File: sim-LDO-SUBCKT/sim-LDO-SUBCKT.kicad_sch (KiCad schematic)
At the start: 10 parts, among them U1 TLV76701DRVx

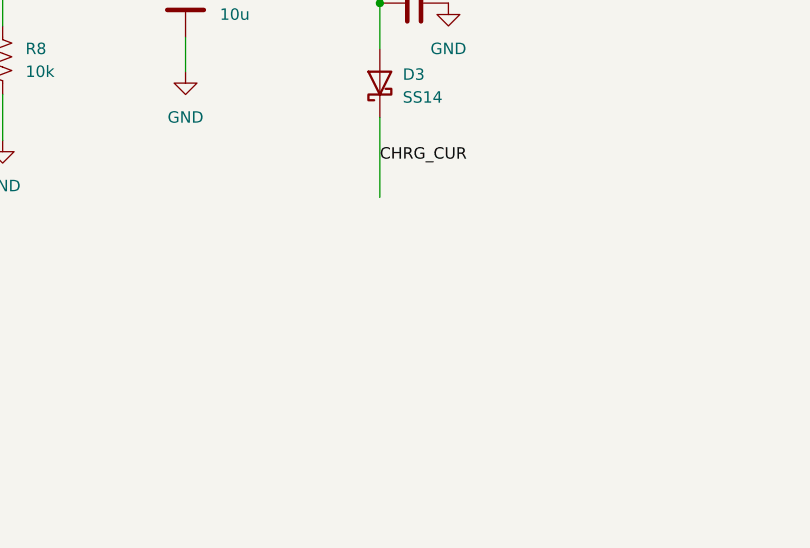
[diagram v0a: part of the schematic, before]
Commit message: simulations fixed with solid model files, results documented
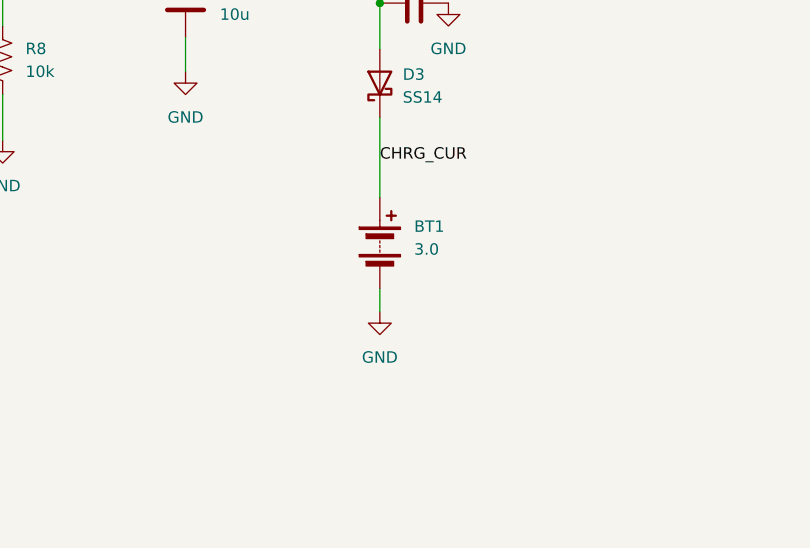
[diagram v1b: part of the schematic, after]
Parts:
- added BT1: 3.0, symbol Device:Battery
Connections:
- net CHRG_CUR: now also BT1.1 (+)
- net GND: now also BT1.2 (-)
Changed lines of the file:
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@@
+	(wire
+		(pts
+			(xy 175.26 127) (xy 175.26 129.54)
+		)
+		(stroke
+			(width 0)
+			(type default)
+		)
+	)
 	(wire
 		(pts
@@
 			)
 		)
-		(property "Sim.Library" "models/TLV767.txt"
+		(property "Sim.Library" "models/TLV76701P_ngspice.lib"
+			(at 116.84 91.44 0)
+			(hide yes)
+			(show_name no)
+			(do_not_autoplace no)
+			(effects
+				(font
+					(size 1.27 1.27)
+				)
+			)
+		)
+		(property "Sim.Name" "TLV76701_TRANS"
+			(at 116.84 91.44 0)
+			(hide yes)
+			(show_name no)
+			(do_not_autoplace no)
+			(effects
+				(font
+					(size 1.27 1.27)
+				)
+			)
+		)
+		(property "Sim.Device" "SUBCKT"
+			(at 116.84 91.44 0)
+			(hide yes)
+			(show_name no)
+			(do_not_autoplace no)
+			(effects
+				(font
+					(size 1.27 1.27)
+				)
+			)
+		)
+		(property "Sim.Pins" "1=VOUT 2=FB 3=GND 4=EN 6=VIN"
 			(at 116.84 91.44 0)
 			(hide yes)
@@
 	)
 	(symbol
+		(lib_id "power:GND")
+		(at 175.26 129.54 0)
+		(unit 1)
+		(body_style 1)
+		(exclude_from_sim no)
+		(in_bom yes)
+		(on_board yes)
+		(in_pos_files yes)
+		(dnp no)
+		(fields_autoplaced yes)
+		(property "Reference" "#PWR06"
+			(at 175.26 135.89 0)
+			(hide yes)
+			(show_name no)
+			(do_not_autoplace no)
+			(effects
+				(font
+					(size 1.27 1.27)
+				)
+			)
+		)
+		(property "Value" "GND"
+			(at 175.26 134.62 0)
+			(show_name no)
+			(do_not_autoplace no)
+			(effects
+				(font
+					(size 1.27 1.27)
+				)
+			)
+		)
+		(property "Footprint" ""
+			(at 175.26 129.54 0)
+			(hide yes)
+			(show_name no)
+			(do_not_autoplace no)
+			(effects
+				(font
+					(size 1.27 1.27)
+				)
+			)
+		)
+		(property "Datasheet" ""
+			(at 175.26 129.54 0)
+			(hide yes)
+			(show_name no)
+			(do_not_autoplace no)
+			(effects
+				(font
+					(size 1.27 1.27)
+				)
+			)
+		)
+		(property "Description" "Power symbol creates a global label with name \"GND\" , ground"
+			(at 175.26 129.54 0)
+			(hide yes)
+			(show_name no)
+			(do_not_autoplace no)
+			(effects
+				(font
+					(size 1.27 1.27)
+				)
+			)
+		)
+		(pin "1"
+		)
+		(instances
+			(project "sim-LDO-SUBCKT"
+				(path "/d4bc50a2-e541-43a2-bfb4-d9a873a3012e"
+					(reference "#PWR06")
+					(unit 1)
+				)
+			)
+		)
+	)
+	(symbol
 		(lib_id "Device:R_US")
 		(at 162.56 85.09 270)
@@
 					(unit 1)
 				)
+			)
+		)
+	)
+	(symbol
+		(lib_id "Device:Battery")
+		(at 175.26 121.92 0)
+		(unit 1)
+		(body_style 1)
+		(exclude_from_sim no)
+		(in_bom yes)
+		(on_board yes)
+		(in_pos_files yes)
+		(dnp no)
+		(fields_autoplaced yes)
+		(property "Reference" "BT1"
+			(at 179.07 120.0784 0)
+			(show_name no)
+			(do_not_autoplace no)
+			(effects
+				(font
+					(size 1.27 1.27)
+				)
+				(justify left)
+			)
+		)
+		(property "Value" "3.0"
+			(at 179.07 122.6184 0)
+			(show_name no)
+			(do_not_autoplace no)
+			(effects
+				(font
+					(size 1.27 1.27)
+				)
+				(justify left)
+			)
+		)
+		(property "Footprint" ""
+			(at 175.26 120.396 90)
+			(hide yes)
+			(show_name no)
+			(do_not_autoplace no)
+			(effects
+				(font
+					(size 1.27 1.27)
+				)
+			)
+		)
+		(property "Datasheet" ""
+			(at 175.26 120.396 90)
+			(hide yes)
+			(show_name no)
+			(do_not_autoplace no)
+			(effects
+				(font
+					(size 1.27 1.27)
+				)
+			)
+		)
+		(property "Description" "Multiple-cell battery"
+			(at 175.26 121.92 0)
+			(hide yes)
+			(show_name no)
+			(do_not_autoplace no)
+			(effects
+				(font
+					(size 1.27 1.27)
+				)
+			)
+		)
+		(property "Sim.Device" "V"
+			(at 175.26 121.92 0)
+			(hide yes)
+			(show_name no)
+			(do_not_autoplace no)
+			(effects
+				(font
+					(size 1.27 1.27)
+				)
+			)
+		)
+		(property "Sim.Type" "DC"
+			(at 175.26 121.92 0)
+			(hide yes)
+			(show_name no)
+			(do_not_autoplace no)
+			(effects
+				(font
+					(size 1.27 1.27)
+				)
+			)
+		)
+		(property "Sim.Pins" "1=+ 2=-"
+			(at 175.26 121.92 0)
+			(hide yes)
+			(show_name no)
+			(do_not_autoplace no)
+			(effects
+				(font
+					(size 1.27 1.27)
+				)
+			)
+		)
+		(pin "2"
+		)
+		(pin "1"
+		)
+		(instances
+			(project "sim-LDO-SUBCKT"
+				(path "/d4bc50a2-e541-43a2-bfb4-d9a873a3012e"
+					(reference "BT1")
+					(unit 1)
+				)
